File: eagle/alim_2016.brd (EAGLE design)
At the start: 90 x 50 mm, 57 parts, among them J1 AVR_SPI_PRG_6PTH, J2 AVR_SPI_PRG_6PTH, U1 3.3V, U2 LM2678S-5.0, U4 LM2596S-ADJ, U5 ATTINY85-20SU, U6 ATMEGA328P_TQFP

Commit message: more cleanup
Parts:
- moved C1 10.6 mm to (77.7, 13.6)
- moved C2 5.40 mm to (73.3, 8.38)
- moved U1 4.94 mm to (79.6, 8.64)
- moved U4 2.62 mm to (71.4, 41.8), turned to 90 degrees
- moved D3 0.77 mm to (43.8, 36.4)
- moved R14 0.77 mm to (42.9, 41.8)
- moved R15 0.77 mm to (42.9, 39.6)
- moved R16 0.77 mm to (41.9, 36.4)
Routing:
- net N$1: track 26.7 -> 0.00 mm
- net 12V: track 105.5 -> 112.8 mm
- net 5.0V: track 111.4 -> 107.3 mm, vias 3 -> 2
- net GND: track 0.00 -> 2.49 mm
- net N$12: track 0.00 -> 2.41 mm
- net N$5: track 8.52 -> 7.70 mm
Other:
- board text added: "Alimentation"
- board text added: "NantRobot 2016"

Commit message: rearrange stuff
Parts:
- moved C3 9.62 mm to (40.6, 22.5)
- moved R1 1.84 mm to (46.2, 31.1), turned to 90 degrees
- moved Q1 0.76 mm to (42.3, 26.0)
- moved C4 0.40 mm to (36.5, 22.5)
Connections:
- net N$29 renamed SW
- net N$30 renamed BOOST
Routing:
- net 5.0V: track 107.3 -> 51.8 mm
- net RESET: track 27.4 -> 31.5 mm

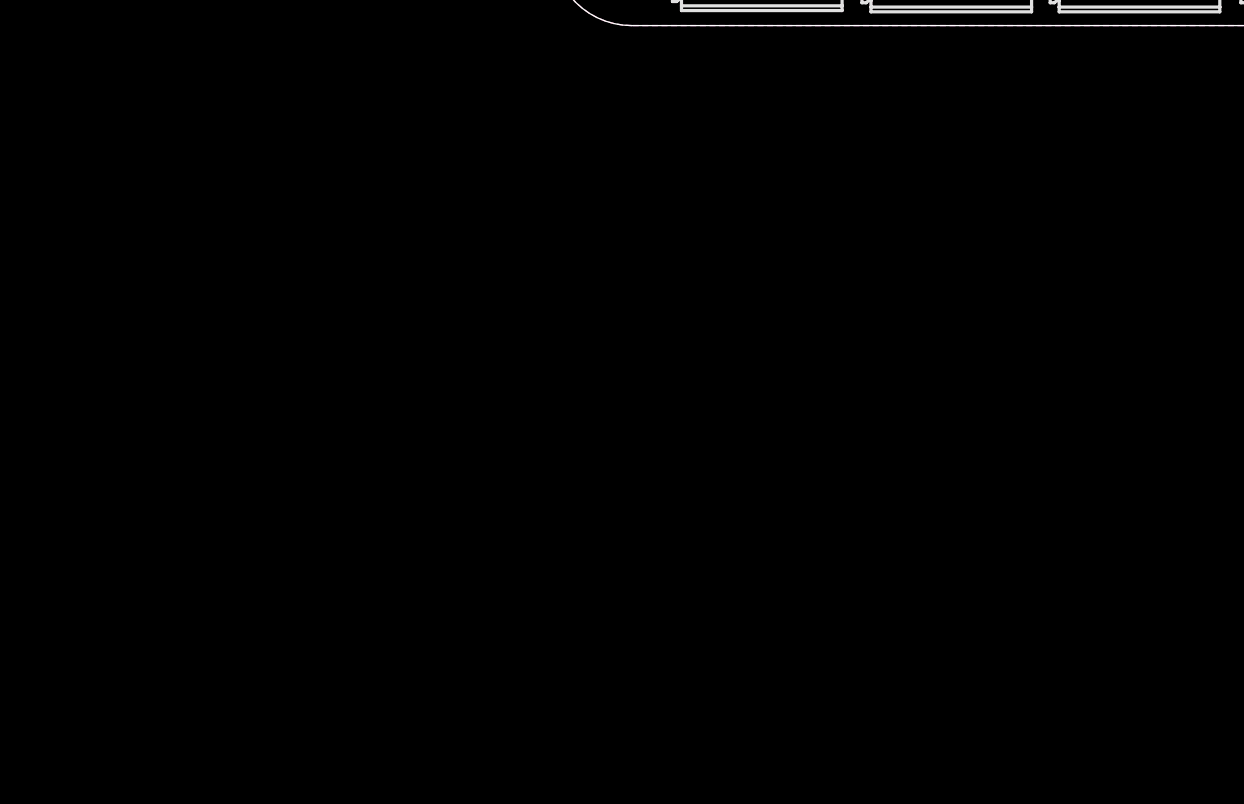
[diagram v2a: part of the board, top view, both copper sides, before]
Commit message: add new switching regulator
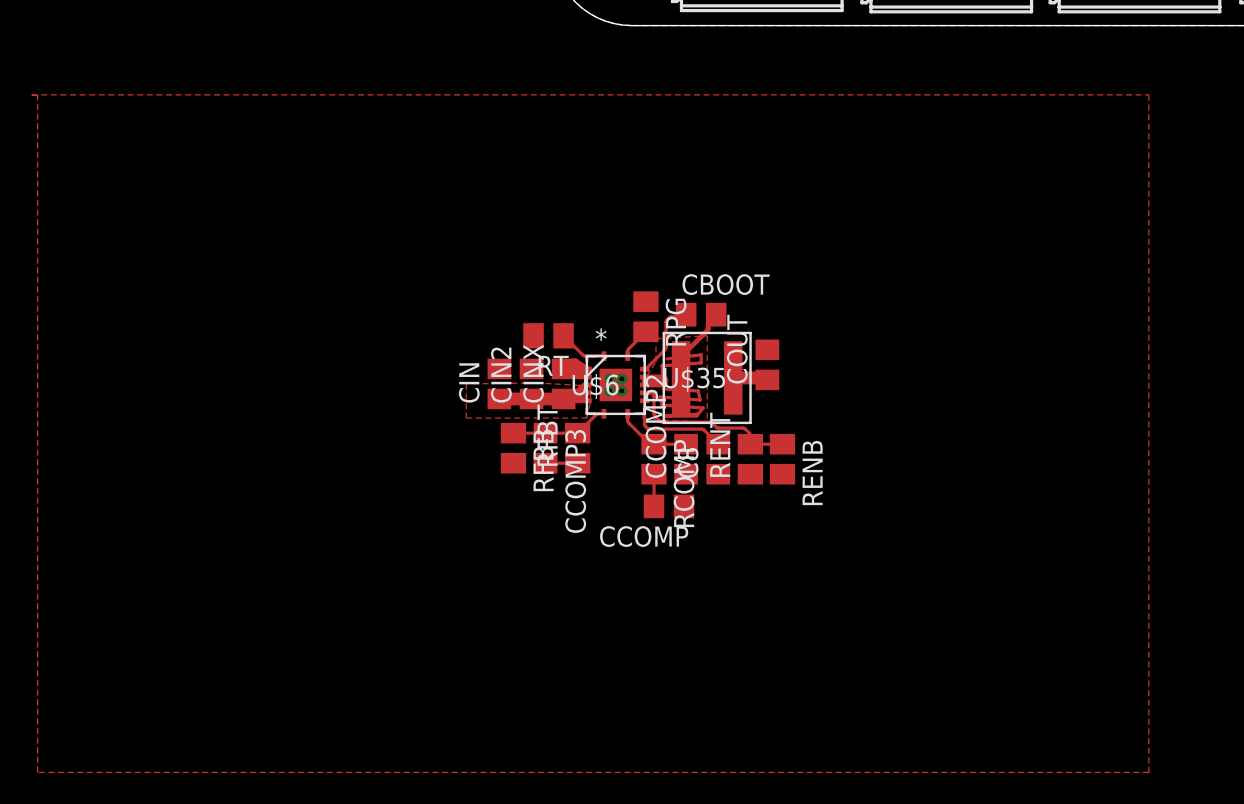
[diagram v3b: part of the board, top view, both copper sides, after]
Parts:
- added C8: 1.8nF, rcl:C0805
- added CBOOT: 100nF, rcl:C0805
- added CCOMP: 39nF, rcl:C0805
- added CCOMP2: 82pF, rcl:C0805
- added CCOMP3: 390pF, rcl:C0805
- added CIN, CIN2: 10uF, rcl:C0805
- added CINX: 4.7uF, rcl:C0805
- added COUT: 22uF, rcl:C0805
- added RCOMP: 1.21K, resistor:M0805
- added RENB: 7.5K, resistor:M0805
- added RENT: 52.3K, resistor:M0805
- added RFBB: 2.21K, resistor:M0805
- added RFBT: 16.2K, resistor:M0805
- added RPG: 48.7K, resistor:M0805
- added RT: 59K, resistor:M0805
- added U$35: 2.2uH, alim:XAL5030
- added U$6: TPS54821RHLR, alim:S-PVQFN-N14
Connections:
- new net COMP: CCOMP2.2, RCOMP.1, U$6.8
- new net EN: RENB.1, RENT.2, U$6.10
- new net N$30: CCOMP.2, RCOMP.2
- new net N$31: CBOOT.1, U$6.13
- new net N$35: RPG.2, U$6.14
- new net PH: CBOOT.2, U$35.1, U$6.11, U$6.12
- new net RTCLK: RT.1, U$6.1
- new net SSTR: C8.2, U$6.9
- new net VSENSE: CCOMP3.1, RFBB.1, RFBT.2, U$6.7
- net 12V: now also CIN.1, CIN2.1, CINX.1, RENT.1, RPG.1, U$6.4, U$6.5, U$6.6
- net 5.0V: now also CCOMP3.2, COUT.1, RFBT.1, U$35.2
- net GND: now also C8.1, CCOMP.1, CCOMP2.1, CIN.2, CIN2.2, CINX.2, COUT.2, RENB.2, RFBB.2, RT.2, U$6.15, U$6.2, U$6.3
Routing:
- net PH: track 0.00 -> 26.7 mm
- net EN: track 0.00 -> 11.1 mm
- net 12V: track 112.7 -> 123.7 mm
- net SSTR: track 0.00 -> 6.68 mm
- net VSENSE: track 0.00 -> 6.22 mm
- net N$31: track 0.00 -> 5.05 mm
- net COMP: track 0.00 -> 4.74 mm
- net GND: track 2.49 -> 6.74 mm
- net 5.0V: track 51.8 -> 56.1 mm
- net RTCLK: track 0.00 -> 3.18 mm
- net N$30: track 0.00 -> 2.03 mm
- net N$35: track 0.00 -> 2.01 mm
- added copper zone on layer 1, net 12V
- added copper zone on layer 1, net PH

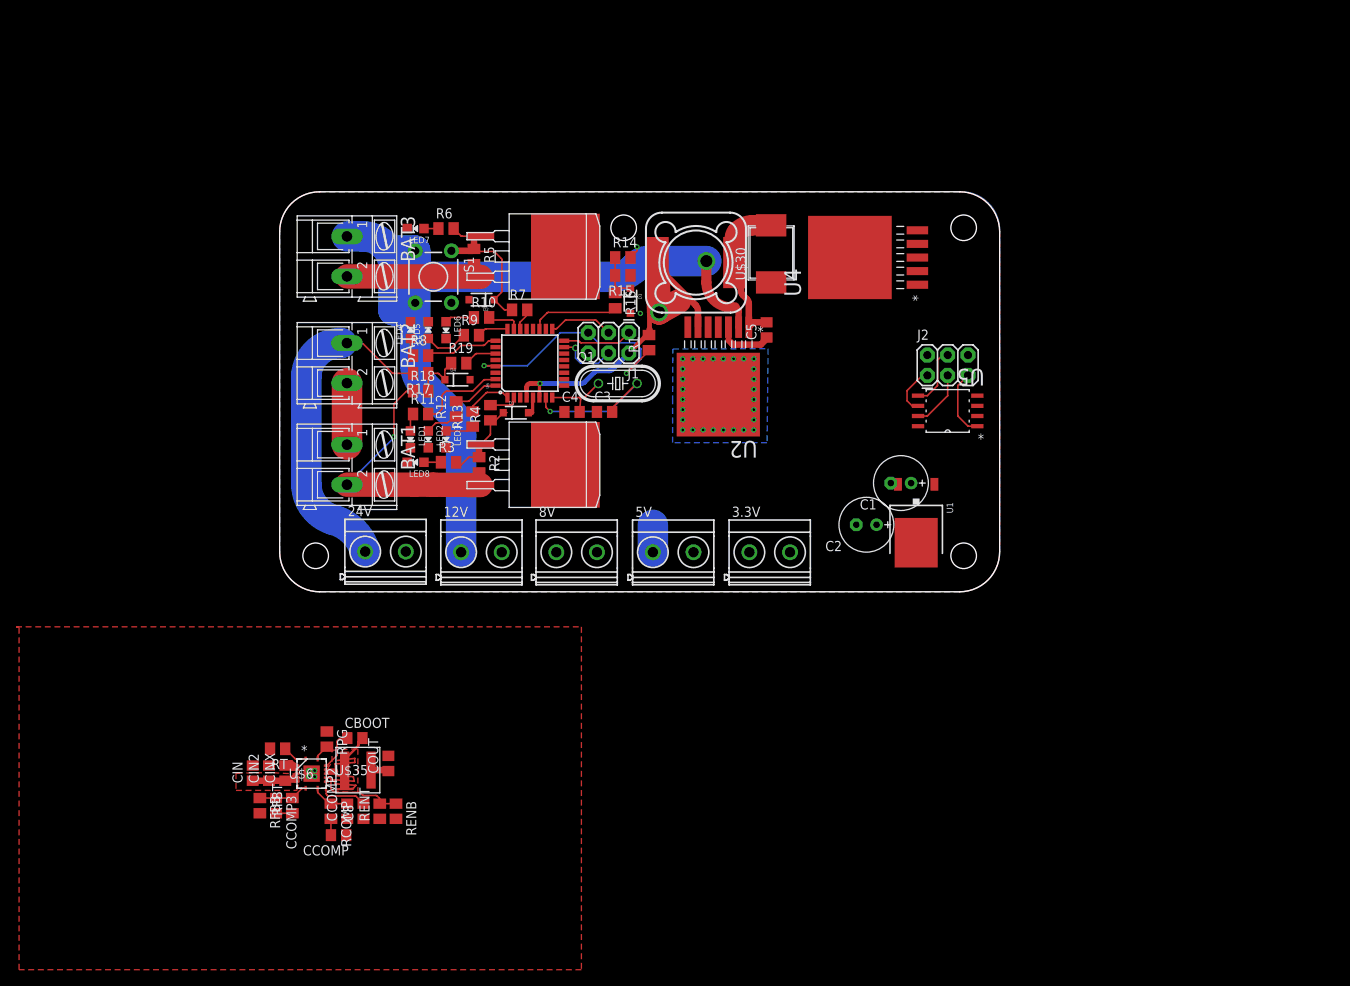
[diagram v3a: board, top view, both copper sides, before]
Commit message: route TPS chip
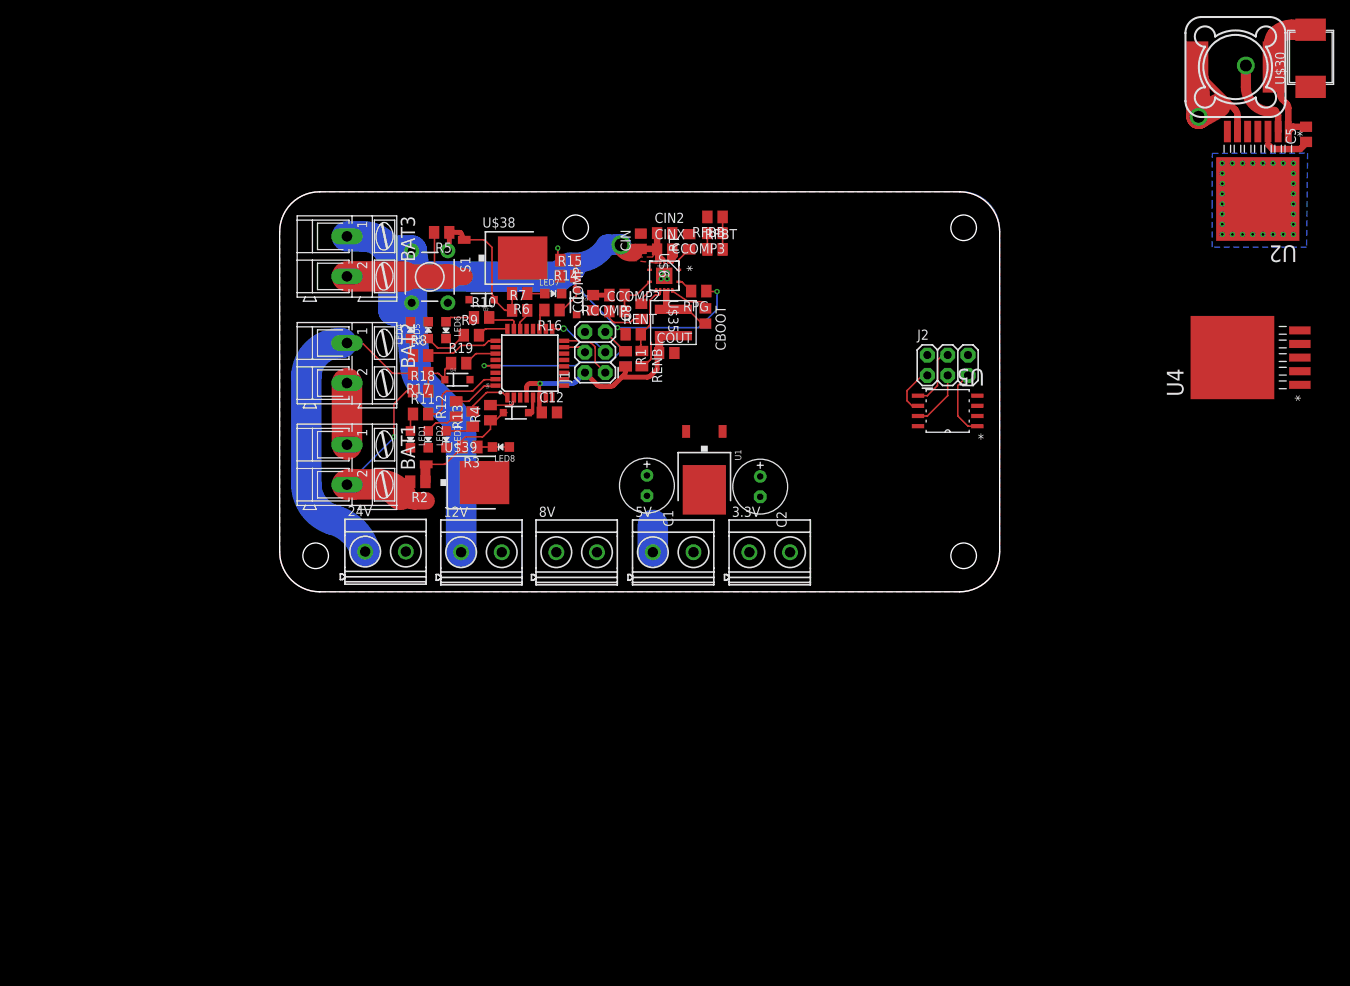
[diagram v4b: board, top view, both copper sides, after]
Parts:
- removed C3, C4: (no value), rcl:C0805
- removed Q1: (no value), crystal:HC49/S
- removed U$19, U$20: CSD19536KTT, alim:TO263-KTT
- added C12: 0.1uF, rcl:C0805
- added U$38, U$39: IRFR8314TRPBF, alim:DPACK_1
- moved RFBB 93.0 mm to (54.4, 46.9), turned to 180 degrees
- moved CCOMP3 90.2 mm to (54.4, 44.8), turned to 180 degrees
- moved RFBT 87.3 mm to (54.4, 42.8), turned to 0 degrees
- moved CIN2 83.7 mm to (48.1, 44.8), turned to 0 degrees
- moved CIN 82.3 mm to (45.1, 43.8)
- moved RT 81.6 mm to (51.2, 43.8), turned to 90 degrees
- moved CINX 80.8 mm to (48.1, 42.8), turned to 0 degrees
- moved U$6 76.3 mm to (48.1, 39.5), turned to 270 degrees
- moved CCOMP 73.8 mm to (39.2, 36.1), turned to 90 degrees
- moved RCOMP 73.8 mm to (42.2, 37.1), turned to 180 degrees
- moved RPG 72.8 mm to (52.4, 37.6), turned to 180 degrees
- moved U$29 71.7 mm to (119.5, 65.6)
- moved U$30 71.7 mm to (128.7, 66.9)
- moved C5 71.7 mm to (128.3, 57.2)
- moved U2 71.7 mm to (122.3, 49.2)
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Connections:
- removed net N$6: C3.2, Q1.2, U6.7
- removed net N$7: C4.2, Q1.1, U6.8
- net 5.0V: now also C12.1
- net BAT12_CUT: now also U$38.1; no longer U$19.1
- net BAT24_CUT: now also U$39.1; no longer U$20.1
- net GND: now also C12.2, U$38.PAD, U$39.PAD; no longer C3.1, C4.1, U$19.TAB, U$20.TAB
- net N$13: now also U$38.3; no longer U$19.3
- net N$8: now also U$39.3; no longer U$20.3
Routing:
- net 12V: track 123.7 -> 148.9 mm, vias 2 -> 5
- net PH: track 26.7 -> 8.45 mm
- net N$6: track 19.4 -> 4.50 mm, vias 1 -> 0
- net GND: track 6.74 -> 16.4 mm, vias 29 -> 32
- net N$27: track 11.1 -> 2.58 mm
- net N$7: track 8.34 -> 0.00 mm
- net N$8: track 34.5 -> 27.9 mm
- net N$13: track 18.3 -> 24.4 mm
- net RESET: track 31.5 -> 26.2 mm, vias 2 -> 1
- net N$4: track 7.64 -> 2.85 mm, vias 1 -> 0
- net BAT24_CUT: track 11.4 -> 15.8 mm
- net SSTR: track 6.68 -> 2.86 mm
- net EN: track 11.1 -> 8.88 mm
- net N$9: track 2.13 -> 3.97 mm
- net VSENSE: track 6.22 -> 4.57 mm
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- removed copper zone on layer 1, net PH

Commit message: cleanup
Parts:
- removed 8V: MKDSN1,5/2-5,08, con-phoenix-508:MKDSN1,5/2-5,08
- removed C5: 10n, rcl:C0805
- removed J2: AVR_SPI_PRG_6PTH, SparkFun-Connectors:2X3
- removed U$29: SRR1260, alim:12.5X12.5
- removed U$30: SBRS8340, alim:SMC
- removed U2: LM2678S-5.0, alim:TO127P1435X457-8N
- removed U5: ATTINY85-20SU, alim:SOIC127P798X216-8N
- added 5V1, 5V2, 5V3, 5V4: MKDSN1,5/2-5,08, con-phoenix-508:MKDSN1,5/2-5,08
- added SG1: F/CM12P, buzzer:F/CM12P
- LED2, LED5: value YELLOW -> YLW
- LED3, LED6: value GREEN -> GRN
- moved C1 35.8 mm to (62.0, 45.3), turned to 0 degrees
- moved 3.3V 33.7 mm to (71.5, 37.1), turned to 90 degrees
- moved U4 29.1 mm to (91.4, 37.8)
- moved U1 22.6 mm to (62.0, 36.0)
- moved RFBB 15.2 mm to (54.0, 31.6)
- moved C2 13.5 mm to (61.8, 26.6), turned to 180 degrees
- moved CCOMP3 11.4 mm to (56.1, 33.5), turned to 0 degrees
- moved RFBT 7.55 mm to (56.1, 35.4), turned to 180 degrees
- moved RENT 0.37 mm to (44.3, 31.8)
- moved COUT 0.28 mm to (48.6, 29.7)
- moved 5V 0.17 mm to (49.1, 5.08)
- moved 12V 0.16 mm to (25.3, 5.08)
- moved CBOOT 0.13 mm to (53.2, 34.6)
- moved RENB 0.13 mm to (45.1, 29.1)
- moved 24V 0.11 mm to (13.3, 5.08)
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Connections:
- removed net BOOST: C5.1, U2.3
- removed net N$39: J2.1, U5.6
- removed net N$40: J2.4, U5.5
- removed net N$41: J2.3, U5.7
- removed net N$42: J2.5, U5.1
- removed net SW: C5.2, U$29.P$1, U$30.2, U2.1
- removed net VCC: U5.8
- net 12V: no longer U2.2
- net 5.0V: now also 5V1.1, 5V2.1, 5V3.1, 5V4.1; no longer J2.2, U$29.P$2, U2.6
- net GND: now also 5V1.2, 5V2.2, 5V3.2, 5V4.2; no longer 8V.2, J2.6, U$30.1, U2.4, U2.8
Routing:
- net 5.0V: track 55.7 -> 147.1 mm, vias 2 -> 3
- net VSENSE: track 4.57 -> 41.2 mm, vias 0 -> 2
- net SW: track 19.4 -> 0.00 mm
- net N$1: track 0.00 -> 18.4 mm
- net N$42: track 8.57 -> 0.00 mm
- net N$40: track 7.67 -> 0.00 mm
- net N$41: track 7.30 -> 0.00 mm
- net BOOST: track 7.08 -> 0.00 mm
- net 12V: track 148.9 -> 142.0 mm, vias 5 -> 4
- net GND: track 16.4 -> 22.8 mm, vias 32 -> 4
- net N$39: track 6.23 -> 0.00 mm
- net N$6: track 4.50 -> 0.00 mm
- net N$8: track 27.9 -> 31.3 mm
- net N$9: track 3.97 -> 1.90 mm
- net N$12: track 2.03 -> 0.00 mm
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- added copper zone on layer 16, net 12V
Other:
- board size 90 x 50 mm -> 77 x 50 mm
